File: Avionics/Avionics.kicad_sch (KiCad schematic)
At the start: 53 parts, among them J1 Conn_02x03_Odd_Even, J2 USB_C_Receptacle_USB2.0_16P, Q1 AO3401A, SW1 SW_SPST, U1 ATmega328P-A, U2 ADXL343, U3 CH340N, U4 MPL3115A2, U5 TP4057, U6 XC6206PxxxMR, Y1 Crystal_GND24

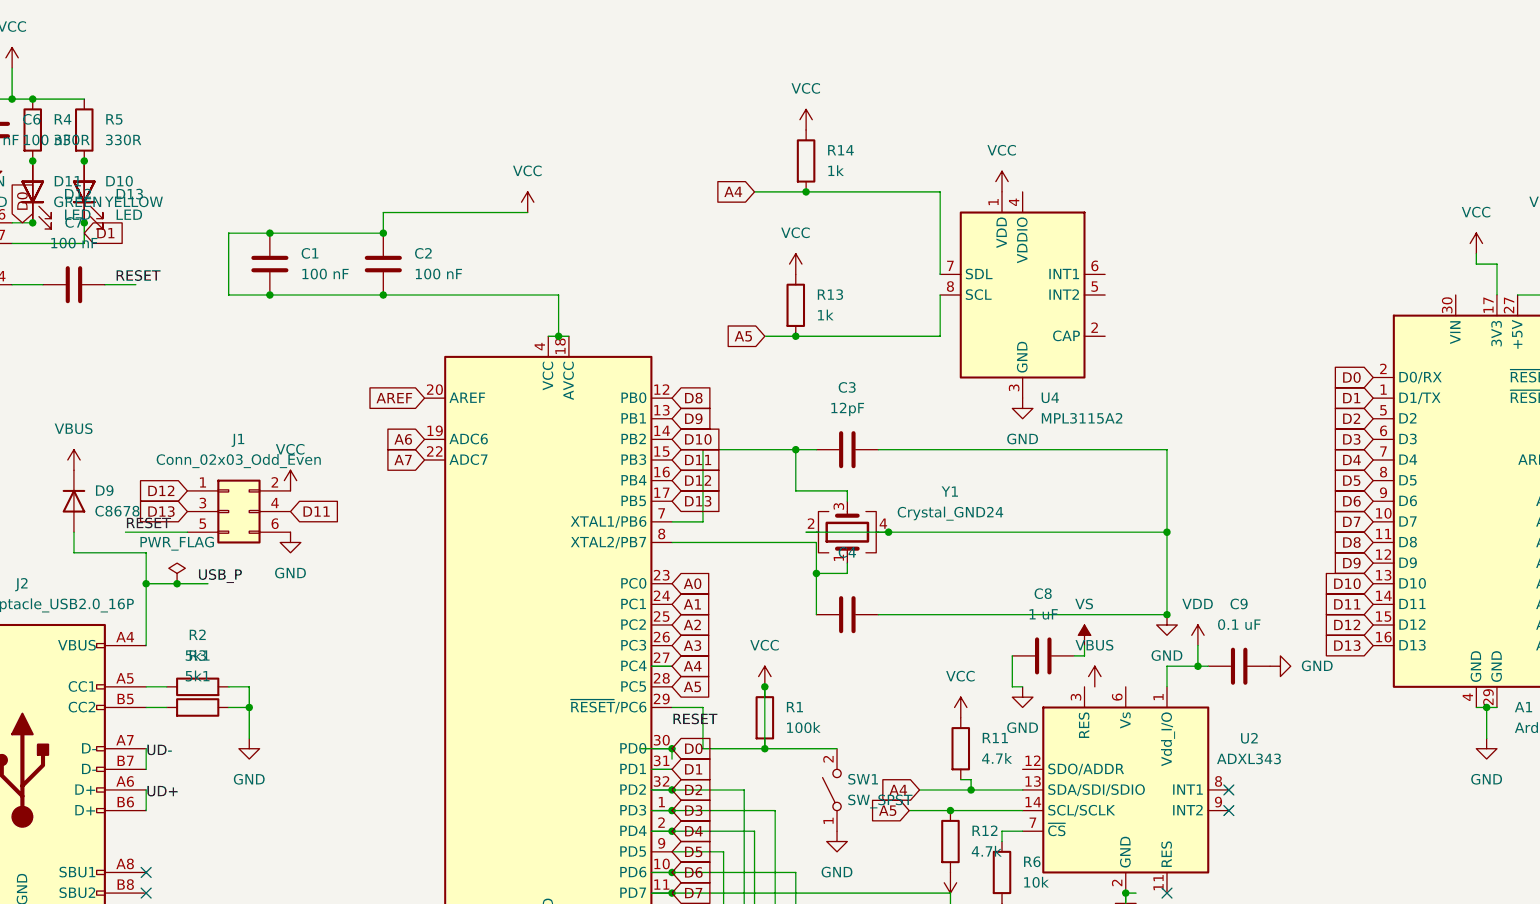
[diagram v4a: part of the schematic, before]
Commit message: Almost done
Basically just need to convert everything to JLCPCB components now, and then I should be good to go.
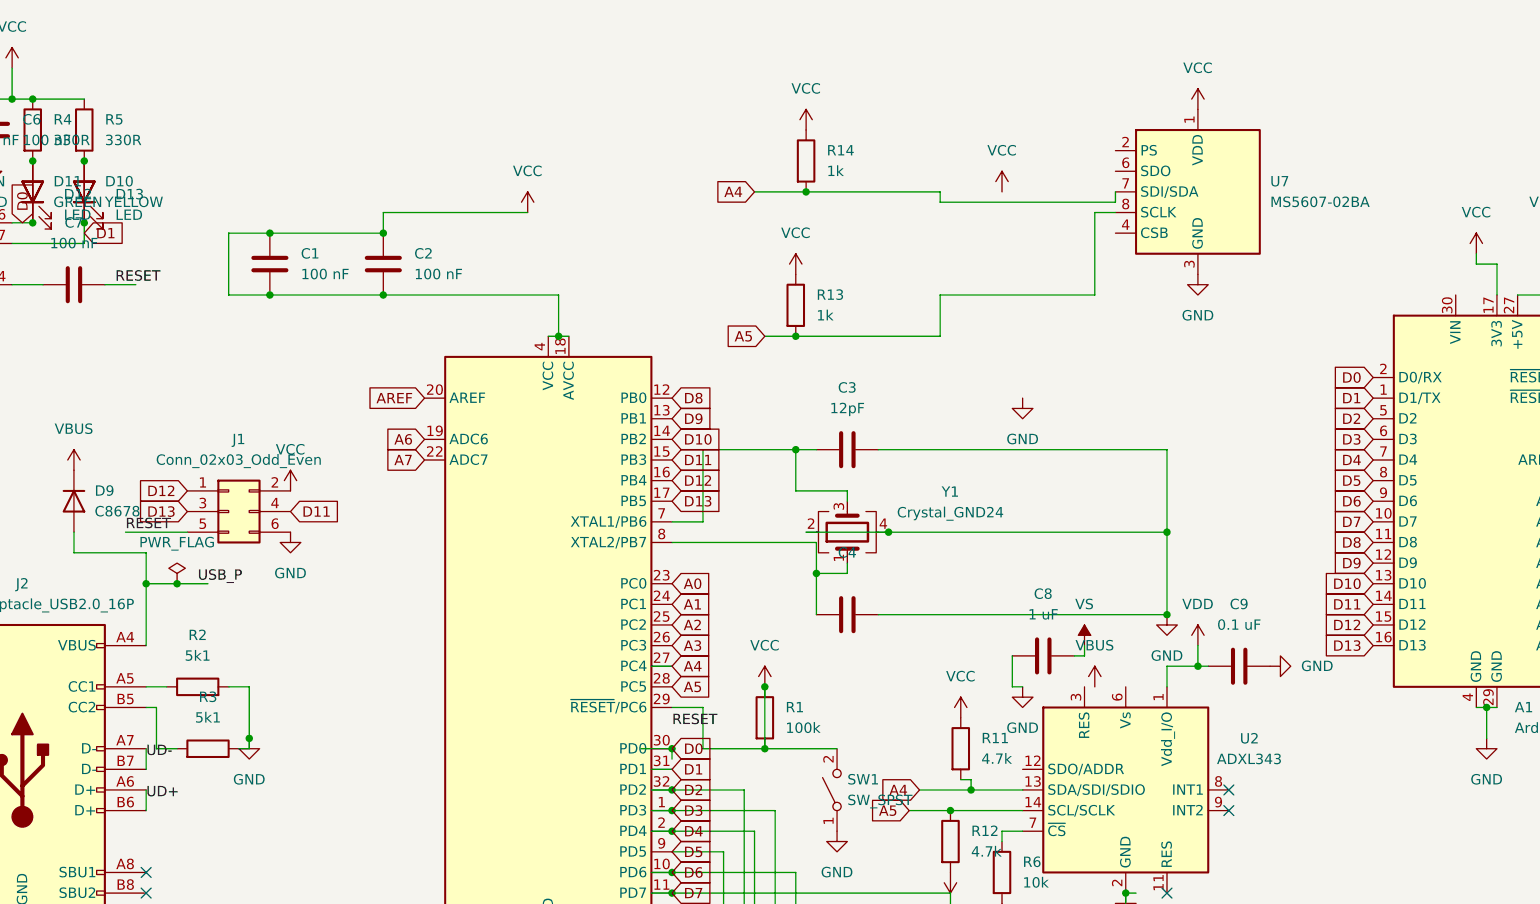
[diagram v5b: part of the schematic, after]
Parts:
- removed U4: MPL3115A2, Package_LGA:NXP_LGA-8_3x5mm_P1.25mm_H1.1mm, symbol Sensor_Pressure:MPL3115A2
- added U7: MS5607-02BA, Package_LGA:LGA-8_3x5mm_P1.25mm, symbol Sensor_Pressure:MS5607-02BA
- C3, C4: LCSC (none) -> C1792
- D10: LCSC (none) -> C2296
- D11, D15: LCSC (none) -> C2297
- Q1: LCSC (none) -> C15127
- R2, R3: LCSC (none) -> C27834
- U1: LCSC (none) -> C14877
- U2: LCSC (none) -> C579453
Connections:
- net A4: now also U7.7 (SDI/SDA)
- net A5: now also U7.8 (SCLK)
- net GND: now also U7.3 (GND)
- net VCC: now also U7.1 (VDD)
- new net: U7.4 (CSB), U7.5 (CSB)
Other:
- moved on the sheet: R3

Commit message: FINISHED
Final assignments, and shrinked board.
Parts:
- C1, C10, C2, C6, C7, C9: LCSC (none) -> C49678
- C11, C5, C8: LCSC (none) -> C111768
- D1, D2, D3, D4, D5, D6, D7, D8: LCSC (none) -> C5378720
- D11: footprint Diode_SMD:D_SMC_Handsoldering -> Diode_SMD:D_1206_3216Metric_Pad1.42x1.75mm_HandSolder
- D12, D13: LCSC (none) -> C2297
- D14, R1: LCSC (none) -> C101927
- D16, D9: LCSC (none) -> C8678
- J1: LCSC (none) -> C65114
- J2: LCSC (none) -> C2988369
- R10, R6: LCSC (none) -> C17414
- R11, R12: LCSC (none) -> C245341
- R13, R14, R9: LCSC (none) -> C17513
- R4, R5: LCSC (none) -> C3016635
- R7: LCSC (none) -> C416128
- R8: LCSC (none) -> C2889530
- SW1: LCSC (none) -> C318884
- U3: LCSC (none) -> C2977777
- U5: LCSC (none) -> C725791
- U6: LCSC (none) -> C2891841
- Y1: LCSC (none) -> C13738
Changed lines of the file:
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@@
 			)
 		)
-		(property "LCSC" ""
+		(property "LCSC" "C5378720"
 			(at 86.36 152.4 0)
 			(effects
@@
 			)
 		)
-		(property "LCSC" ""
+		(property "LCSC" "C17513"
 			(at 140.97 44.45 0)
 			(effects
@@
 			)
 		)
-		(property "LCSC" ""
+		(property "LCSC" "C17414"
 			(at 166.37 114.3 0)
 			(effects
@@
 			)
 		)
-		(property "LCSC" ""
+		(property "LCSC" "C2889530"
 			(at 252.73 125.73 0)
 			(effects
@@
 			)
 		)
-		(property "LCSC" ""
+		(property "LCSC" "C49678"
 			(at 195.58 88.9 0)
 			(effects
@@
 			)
 		)
-		(property "LCSC" ""
+		(property "LCSC" "C2891841"
 			(at 152.4 172.72 0)
 			(effects
@@
 			)
 		)
-		(property "LCSC" ""
+		(property "LCSC" "C49678"
 			(at 76.2 39.37 0)
 			(effects
@@
 			)
 		)
-		(property "LCSC" ""
+		(property "LCSC" "C5378720"
 			(at 46.99 152.4 0)
 			(effects
@@
 			)
 		)
-		(property "LCSC" ""
+		(property "LCSC" "C8678"
 			(at 106.68 177.8 0)
 			(effects
@@
 			)
 		)
-		(property "LCSC" ""
+		(property "LCSC" "C49678"
 			(at 41.91 22.86 0)
 			(effects
@@
 			)
 		)
-		(property "LCSC" ""
+		(property "LCSC" "C245341"
 			(at 161.29 99.06 0)
 			(effects
@@
 			)
 		)
-		(property "LCSC" ""
+		(property "LCSC" "C17414"
 			(at 102.87 187.96 0)
 			(effects
@@
 			)
 		)
-		(property "LCSC" ""
+		(property "LCSC" "C318884"
 			(at 146.05 104.14 0)
 			(effects
@@
 			)
 		)
-		(property "LCSC" ""
+		(property "LCSC" "C245341"
 			(at 160.02 110.49 0)
 			(effects
@@
 			)
 		)
-		(property "LCSC" ""
+		(property "LCSC" "C2297"
 			(at 53.34 30.48 0)
 			(effects
@@
 			)
 		)
-		(property "LCSC" ""
+		(property "LCSC" "C65114"
 			(at 71.12 69.85 0)
 			(effects
@@
 			)
 		)
-		(property "LCSC" ""
+		(property "LCSC" "C725791"
 			(at 237.49 135.89 0)
 			(effects
@@
 			)
 		)
-		(property "LCSC" ""
+		(property "LCSC" "C17513"
 			(at 219.71 127 0)
 			(effects
@@
 			)
 		)
-		(property "LCSC" ""
+		(property "LCSC" "C5378720"
 			(at 106.68 152.4 0)
 			(effects
@@
 			)
 		)
-		(property "LCSC" ""
+		(property "LCSC" "C111768"
 			(at 168.91 181.61 0)
 			(effects
@@
 			)
 		)
-		(property "LCSC" ""
+		(property "LCSC" "C101927"
 			(at 137.16 95.25 0)
 			(effects
@@
 			)
 		)
-		(property "LCSC" ""
+		(property "LCSC" "C111768"
 			(at 132.08 181.61 0)
 			(effects
@@
 			)
 		)
-		(property "LCSC" ""
+		(property "LCSC" "C5378720"
 			(at 26.67 152.4 0)
 			(effects
@@
 			)
 		)
-		(property "LCSC" ""
+		(property "LCSC" "C111768"
 			(at 171.45 87.63 0)
 			(effects
@@
 			)
 		)
-		(property "LCSC" ""
+		(property "LCSC" "C17513"
 			(at 142.24 26.67 0)
 			(effects
@@
 			)
 		)
-		(property "LCSC" ""
+		(property "LCSC" "C2988369"
 			(at 45.72 101.6 0)
 			(effects
@@
 			)
 		)
-		(property "LCSC" ""
+		(property "LCSC" "C3016635"
 			(at 53.34 22.86 0)
 			(effects
@@
 			)
 		)
-		(property "LCSC" ""
+		(property "LCSC" "C416128"
 			(at 252.73 144.78 0)
 			(effects
@@
 			)
 		)
-		(property "LCSC" ""
+		(property "LCSC" "C49678"
 			(at 52.07 41.91 0)
 			(effects
@@
 			)
 		)
-		(property "LCSC" ""
+		(property "LCSC" "C3016635"
 			(at 46.99 22.86 0)
 			(effects
@@
 			)
 		)
-		(property "LCSC" ""
+		(property "LCSC" "C5378720"
 			(at 66.04 152.4 0)
 			(effects
@@
 			)
 		)
-		(property "LCSC" ""
+		(property "LCSC" "C2297"
 			(at 46.99 30.48 0)
 			(effects
@@
 			)
 		)
-		(property "LCSC" ""
+		(property "LCSC" "C5378720"
 			(at 147.32 152.4 0)
 			(effects
@@
 			)
 		)
-		(property "LCSC" ""
+		(property "LCSC" "C13738"
 			(at 147.32 72.39 0)
 			(effects
@@
 			)
 		)
-		(property "LCSC" ""
+		(property "LCSC" "C5378720"
 			(at 127 152.4 0)
 			(effects
@@
 			)
 		)
-		(property "Footprint" "Diode_SMD:D_SMC_Handsoldering"
+		(property "Footprint" "Diode_SMD:D_1206_3216Metric_Pad1.42x1.75mm_HandSolder"
 			(at 46.99 30.48 0)
 			(effects
@@
 			)
 		)
-		(property "LCSC" ""
+		(property "LCSC" "C2977777"
 			(at 34.29 36.83 0)
 			(effects
@@
 			)
 		)
-		(property "LCSC" ""
+		(property "LCSC" "C8678"
 			(at 52.07 68.58 0)
 			(effects
@@
 			)
 		)
-		(property "LCSC" ""
+		(property "LCSC" "C49678"
 			(at 35.56 22.86 0)
 			(effects
@@
 			)
 		)
-		(property "LCSC" ""
+		(property "LCSC" "C49678"
 			(at 90.17 39.37 0)
 			(effects
@@
 			)
 		)
-		(property "LCSC" ""
+		(property "LCSC" "C101927"
 			(at 223.52 133.35 0)
 			(effects
@@
 			)
 		)
-		(property "LCSC" ""
+		(property "LCSC" "C5378720"
 			(at 167.64 152.4 0)
 			(effects
